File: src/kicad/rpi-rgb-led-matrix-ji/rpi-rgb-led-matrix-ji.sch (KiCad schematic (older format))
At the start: 43 parts, among them J1 Conn_01x02_Male, J2 Conn_02x10_Odd_Even, J3 Screw_Terminal_01x02, J4 Conn_02x08_Odd_Even, J5 Conn_02x08_Odd_Even, J6 Conn_02x08_Odd_Even, P1 Raspberry_Pi_2_3, Q1 DMG2305UX, Q2 DMMT5401, U1 74HCT245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

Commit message: m
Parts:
- C1, C2, C3, C4: DigiKey part number (none) -> 732-8127-1-ND; Mfg part number (none) -> 885012208087
- P1: DigiKey part number (none) -> S7123-ND; Mfg part number (none) -> PPPC202LFBN-RC
- Q1: DigiKey part number (none) -> DMG2305UX-13DICT-ND; Mfg part number (none) -> DMG2305UX-13
- Q2: DigiKey part number (none) -> DMMT5401-FDICT-ND; Mfg part number (none) -> DMMT5401-7-F
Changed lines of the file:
@@
 F 2 "Connector_PinSocket_2.54mm:PinSocket_2x20_P2.54mm_Vertical" H 5450 4350 50  0001 C CNN
 F 3 "https://www.raspberrypi.org/documentation/hardware/raspberrypi/schematics/rpi_SCH_3bplus_1p0_reduced.pdf" H 5450 4350 50  0001 C CNN
+F 4 "S7123-ND" H 0   0   50  0001 C CNN "DigiKey part number"
+F 5 "PPPC202LFBN-RC" H 0   0   50  0001 C CNN "Mfg part number"
 	1    5450 4350
 	1    0    0    -1
@@
 F 1 "100nF" H 8300 4050 50  0000 L CNN
 F 2 "Capacitor_SMD:C_1206_3216Metric_Pad1.42x1.75mm_HandSolder" H 8588 4000 50  0001 C CNN
-F 3 "~" H 8550 4150 50  0001 C CNN
+F 3 "https://katalog.we-online.de/pbs/datasheet/885012208087.pdf" H 8550 4150 50  0001 C CNN
+F 4 "732-8127-1-ND" H 0   0   50  0001 C CNN "DigiKey part number"
+F 5 "885012208087" H 0   0   50  0001 C CNN "Mfg part number"
 	1    8550 4150
 	1    0    0    -1
@@
 F 1 "100nF" H 8700 4050 50  0000 L CNN
 F 2 "Capacitor_SMD:C_1206_3216Metric_Pad1.42x1.75mm_HandSolder" H 8988 4000 50  0001 C CNN
-F 3 "~" H 8950 4150 50  0001 C CNN
+F 3 "https://katalog.we-online.de/pbs/datasheet/885012208087.pdf" H 8950 4150 50  0001 C CNN
+F 4 "732-8127-1-ND" H 0   0   50  0001 C CNN "DigiKey part number"
+F 5 "885012208087" H 0   0   50  0001 C CNN "Mfg part number"
 	1    8950 4150
 	1    0    0    -1
@@
 F 1 "100nF" H 9100 4050 50  0000 L CNN
 F 2 "Capacitor_SMD:C_1206_3216Metric_Pad1.42x1.75mm_HandSolder" H 9388 4000 50  0001 C CNN
-F 3 "~" H 9350 4150 50  0001 C CNN
+F 3 "https://katalog.we-online.de/pbs/datasheet/885012208087.pdf" H 9350 4150 50  0001 C CNN
+F 4 "732-8127-1-ND" H 0   0   50  0001 C CNN "DigiKey part number"
+F 5 "885012208087" H 0   0   50  0001 C CNN "Mfg part number"
 	1    9350 4150
 	1    0    0    -1
@@
 F 1 "100nF" H 9500 4050 50  0000 L CNN
 F 2 "Capacitor_SMD:C_1206_3216Metric_Pad1.42x1.75mm_HandSolder" H 9788 4000 50  0001 C CNN
-F 3 "~" H 9750 4150 50  0001 C CNN
+F 3 "https://katalog.we-online.de/pbs/datasheet/885012208087.pdf" H 9750 4150 50  0001 C CNN
+F 4 "732-8127-1-ND" H 0   0   50  0001 C CNN "DigiKey part number"
+F 5 "885012208087" H 0   0   50  0001 C CNN "Mfg part number"
 	1    9750 4150
 	1    0    0    -1
@@
 F 1 "DMMT5401" H 2650 4050 50  0000 L CNN
 F 2 "Package_TO_SOT_SMD:SOT-23-6" H 2550 3900 50  0001 C CNN
-F 3 "" H 2550 3900 50  0001 C CNN
+F 3 "https://www.diodes.com/assets/Datasheets/ds30437.pdf" H 2550 3900 50  0001 C CNN
+F 4 "DMMT5401-FDICT-ND" H 0   0   50  0001 C CNN "DigiKey part number"
+F 5 "DMMT5401-7-F" H 0   0   50  0001 C CNN "Mfg part number"
 	1    2550 4000
 	-1   0    0    1
@@
 F 1 "DMMT5401" H 3741 4045 50  0000 L CNN
 F 2 "Package_TO_SOT_SMD:SOT-23-6" H 3650 3900 50  0001 C CNN
-F 3 "" H 3650 3900 50  0001 C CNN
+F 3 "https://www.diodes.com/assets/Datasheets/ds30437.pdf" H 3650 3900 50  0001 C CNN
+F 4 "DMMT5401-FDICT-ND" H 0   0   50  0001 C CNN "DigiKey part number"
+F 5 "DMMT5401-7-F" H 0   0   50  0001 C CNN "Mfg part number"
 	2    3650 4000
 	1    0    0    1
@@
 F 1 "DMG2305UX" V 3302 3500 50  0000 C CNN
 F 2 "Package_TO_SOT_SMD:SOT-23" H 3250 3425 50  0001 L CIN
-F 3 "http://www.farnell.com/datasheets/1835997.pdf" H 3050 3500 50  0001 L CNN
+F 3 "https://www.diodes.com/assets/Datasheets/DMG2305UX.pdf" H 3050 3500 50  0001 L CNN
+F 4 "DMG2305UX-13DICT-ND" H 0   0   50  0001 C CNN "DigiKey part number"
+F 5 "DMG2305UX-13" H 0   0   50  0001 C CNN "Mfg part number"
 	1    3050 3500
 	0    -1   -1   0

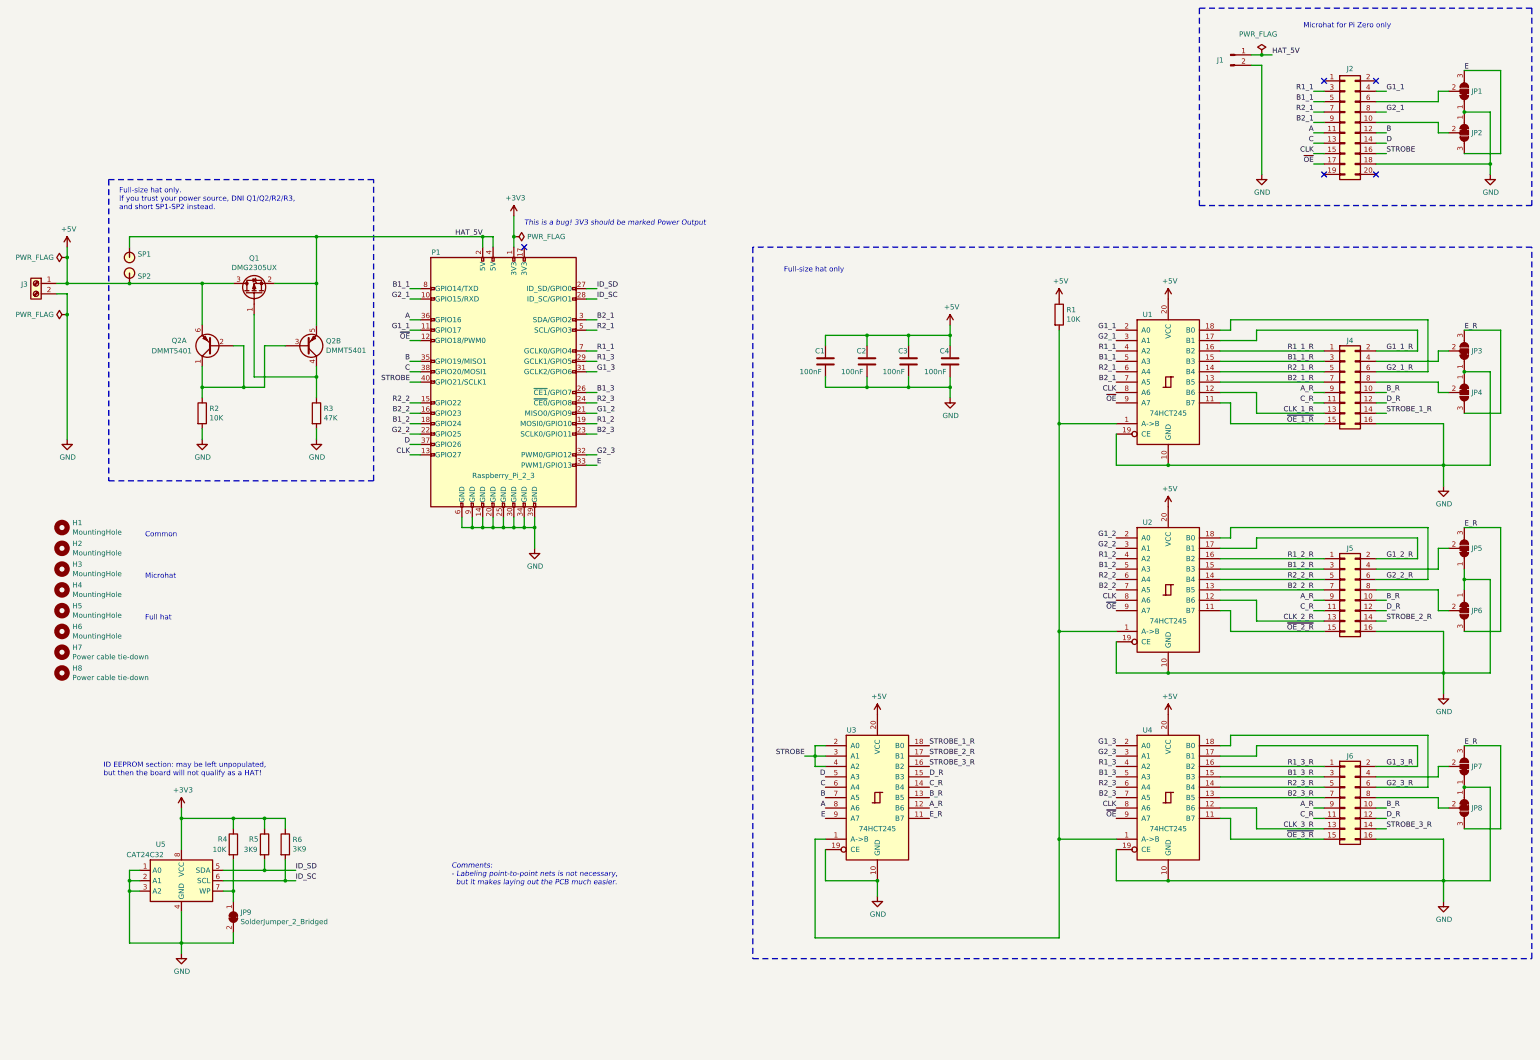
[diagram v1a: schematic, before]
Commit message: fixed g1/g2 inversion, removed virtual diode bypass
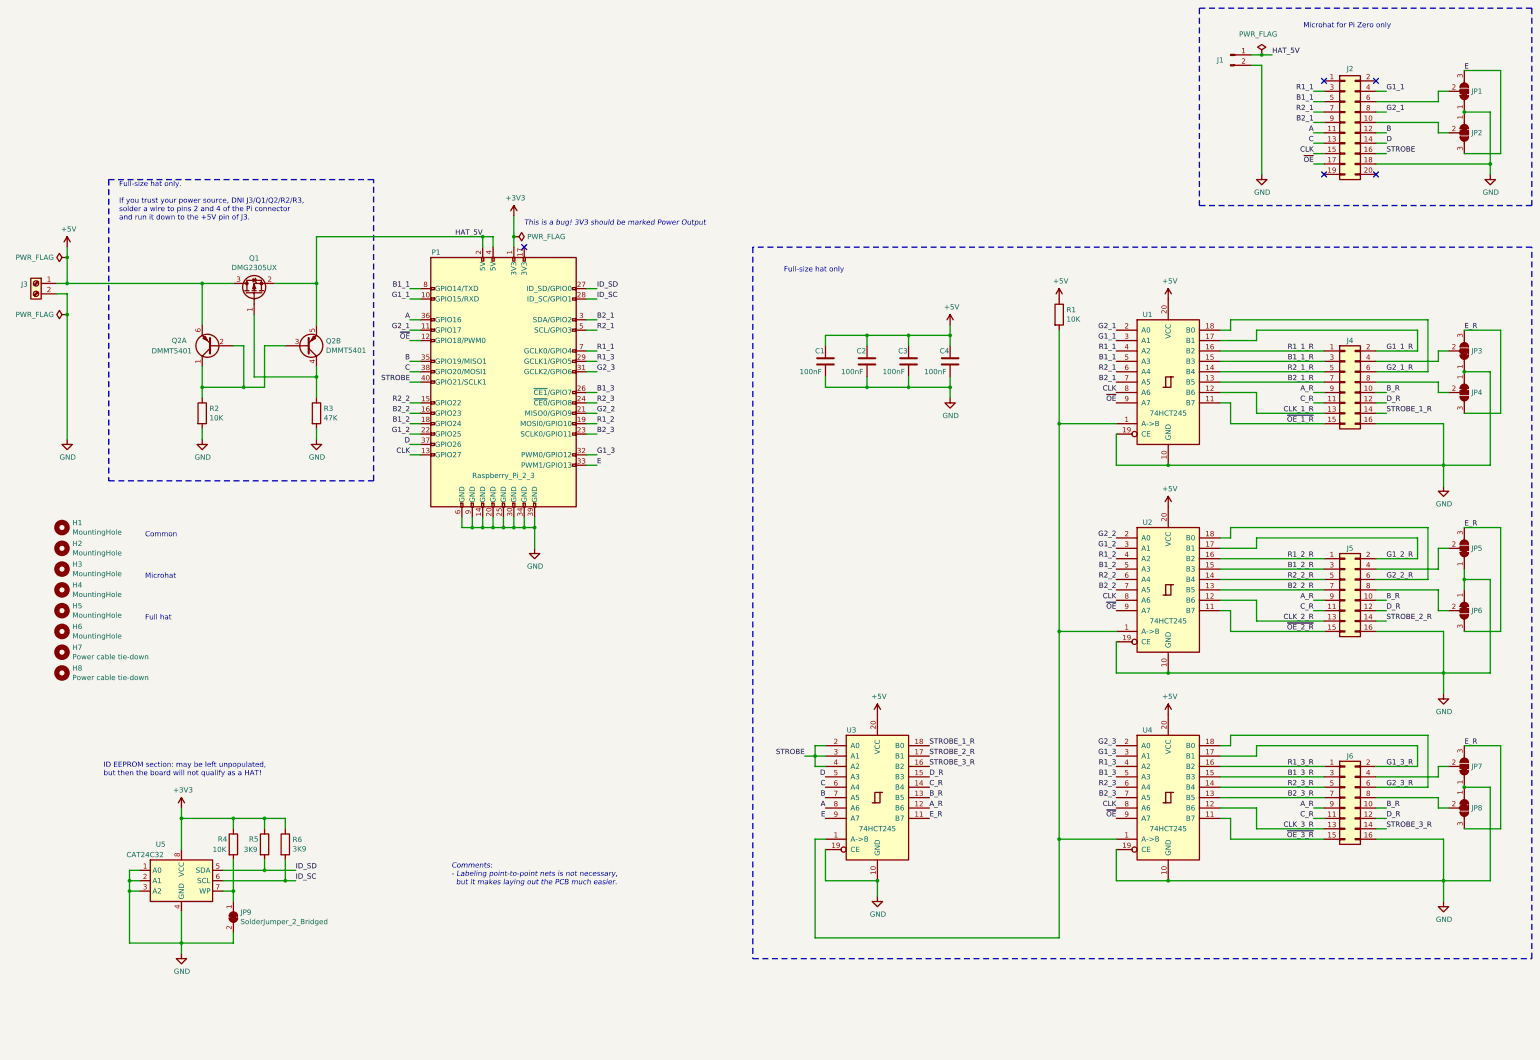
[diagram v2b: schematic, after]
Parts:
- removed SP1, SP2: SP, jicad:smd1mm4pad1, symbol jicad:SP
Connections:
- net G1_1: now also P1.10 (GPIO15/RXD), U1.3 (A1); no longer P1.11 (GPIO17), U1.2 (A0)
- net G1_2: now also P1.22 (GPIO25), U2.3 (A1); no longer P1.21 (MISO0/GPIO9), U2.2 (A0)
- net G1_3: now also P1.32 (PWM0/GPIO12), U4.3 (A1); no longer P1.31 (GCLK2/GPIO6), U4.2 (A0)
- net G2_1: now also P1.11 (GPIO17), U1.2 (A0); no longer P1.10 (GPIO15/RXD), U1.3 (A1)
- net G2_2: now also P1.21 (MISO0/GPIO9), U2.2 (A0); no longer P1.22 (GPIO25), U2.3 (A1)
- net G2_3: now also P1.31 (GCLK2/GPIO6), U4.2 (A0); no longer P1.32 (PWM0/GPIO12), U4.3 (A1)
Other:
- note added: "Full-size hat only.\n\nIf you trust your power source, DNI J3/Q1/Q2/R2/R3,\nsolder a wire to pins 2 and 4 of the Pi connector\nand run it down to the +5V pin of J3."
- note removed: "Full-size hat only.\nIf you trust your power source, DNI Q1/Q2/R2/R3,\nand short SP1-SP2 instead."
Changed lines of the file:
@@
 Sheet 1 1
 Title "Led matrix driver"
-Date "2019-03-15"
-Rev "1.2.2"
+Date "2019-03-24"
+Rev "1.2.3"
 Comp "TLA CONSULTING, LLC"
 Comment1 ""
@@
 Text Label 6350 4050 0    50   ~ 0
 R1_1
-Text Label 4550 3850 2    50   ~ 0
+Text Label 4550 3550 2    50   ~ 0
 G1_1
 Text Label 4550 3450 2    50   ~ 0
 B1_1
-Text Label 4550 3550 2    50   ~ 0
+Text Label 4550 3850 2    50   ~ 0
 G2_1
 Text Label 4550 4350 2    50   ~ 0
@@
 	1    0    0    -1
 $EndComp
+Text Label 11350 3950 2    50   ~ 0
+G1_1
 Text Label 11350 3850 2    50   ~ 0
-G1_1
-Text Label 11350 3950 2    50   ~ 0
 G2_1
 Text Label 11350 4050 2    50   ~ 0
@@
 Text Label 11350 4350 2    50   ~ 0
 B2_1
+Text Label 11350 5950 2    50   ~ 0
+G1_2
 Text Label 11350 5850 2    50   ~ 0
-G1_2
-Text Label 11350 5950 2    50   ~ 0
 G2_2
 Text Label 11350 6050 2    50   ~ 0
@@
 Text Label 11350 6350 2    50   ~ 0
 B2_2
+Text Label 11350 7950 2    50   ~ 0
+G1_3
 Text Label 11350 7850 2    50   ~ 0
-G1_3
-Text Label 11350 7950 2    50   ~ 0
 G2_3
 Text Label 11350 8050 2    50   ~ 0
@@
 Text Label 6350 5150 0    50   ~ 0
 E
+Text Label 4550 4850 2    50   ~ 0
+G1_2
 Text Label 6350 4650 0    50   ~ 0
-G1_2
-Text Label 4550 4850 2    50   ~ 0
 G2_2
 Text Label 6350 4750 0    50   ~ 0
@@
 Text Label 4550 4650 2    50   ~ 0
 B2_2
+Text Label 6350 5050 0    50   ~ 0
+G1_3
 Text Label 6350 4250 0    50   ~ 0
-G1_3
-Text Label 6350 5050 0    50   ~ 0
 G2_3
 Text Label 6350 4150 0    50   ~ 0
@@
 Wire Wire Line
 	1250 3700 1250 4900
-Wire Wire Line
-	3650 2950 1850 2950
-Wire Wire Line
-	1850 2950 1850 3050
-Connection ~ 3650 2950
-$Comp
-L jicad:SP SP1
-U 1 1 5CC3A54B
-P 1850 3050
-F 0 "SP1" V 1918 3128 50  0000 L CNN
-F 1 "SP" H 2027 3004 25  0001 L CNN
-F 2 "jicad:smd1mm4pad1" H 1850 3050 50  0001 C CNN
-F 3 "" H 1850 3050 50  0001 C CNN
-	1    1850 3050
-	0    1    1    0
-$EndComp
-$Comp
-L jicad:SP SP2
-U 1 1 5CC3A7B5
-P 1850 3400
-F 0 "SP2" V 1919 3322 50  0000 R CNN
-F 1 "SP" H 2027 3354 25  0001 L CNN
-F 2 "jicad:smd1mm4pad1" H 1850 3400 50  0001 C CNN
-F 3 "" H 1850 3400 50  0001 C CNN
-	1    1850 3400
-	0    -1   -1   0
-$EndComp
 Wire Notes Line
 	1650 5300 4200 5300
@@
 Wire Notes Line
 	1650 2400 1650 5300
-Text Notes 1750 2700 0    50   ~ 0
-Full-size hat only.\nIf you trust your power source, DNI Q1/Q2/R2/R3,\nand short SP1-SP2 instead.
-Wire Wire Line
-	1250 3400 1850 3400
-Connection ~ 1850 3400
-Wire Wire Line
-	1850 3400 2550 3400
+Text Notes 1750 2800 0    50   ~ 0
+Full-size hat only.\n\nIf you trust your power source, DNI J3/Q1/Q2/R2/R3,\nsolder a wire to pins 2 and 4 of the Pi connector\nand run it down to the +5V pin of J3.
+Wire Wire Line
+	1250 3400 2550 3400
 $EndSCHEMATC
